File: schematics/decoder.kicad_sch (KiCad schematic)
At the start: 3 parts, among them U10 ATF22V10C-7, U11 74HC373, U9 ATF22V10C-7

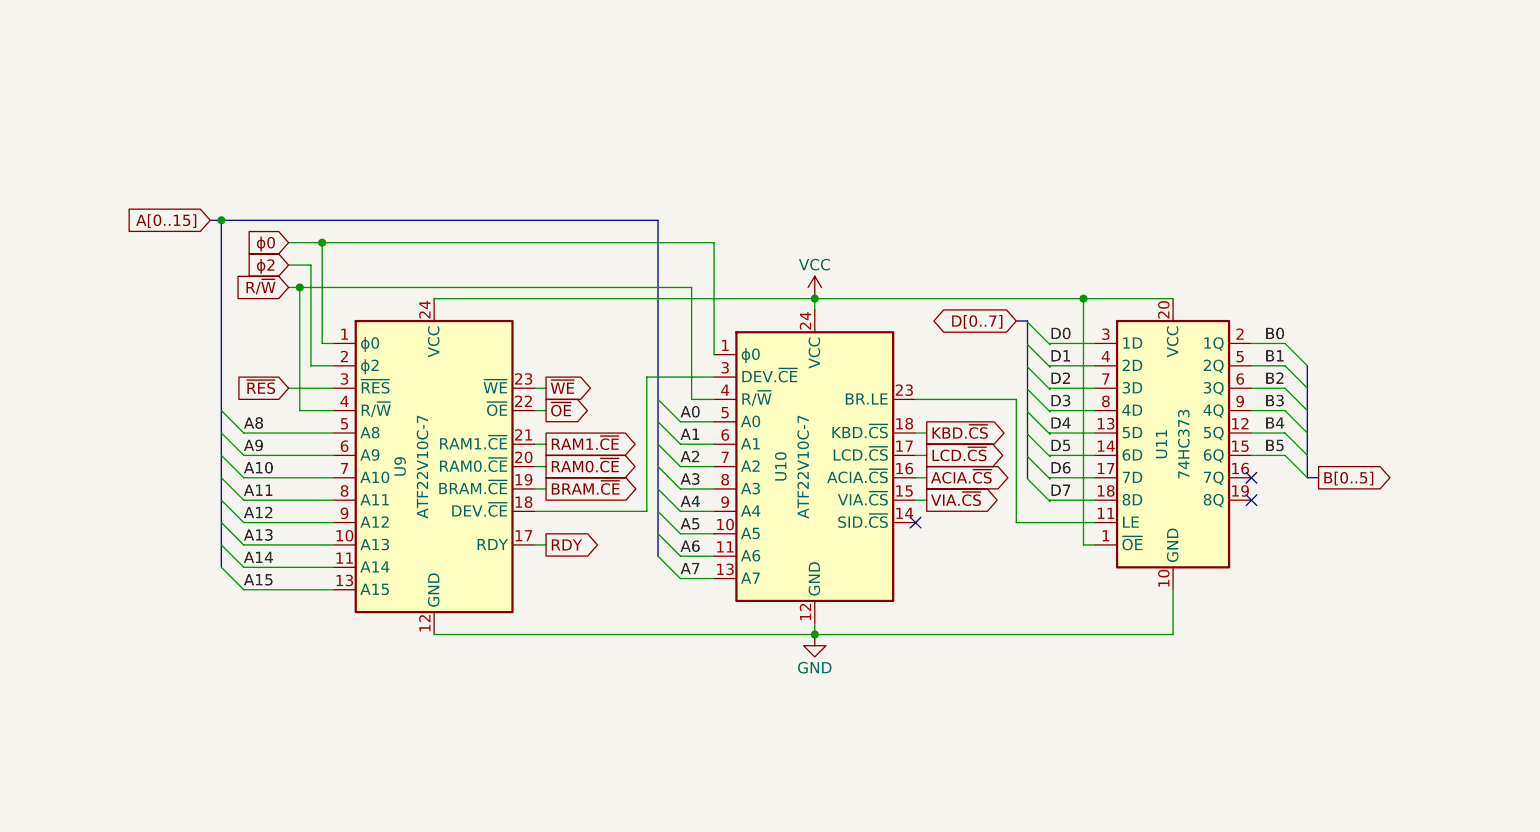
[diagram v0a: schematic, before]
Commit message: added back bus transceiver for devsel
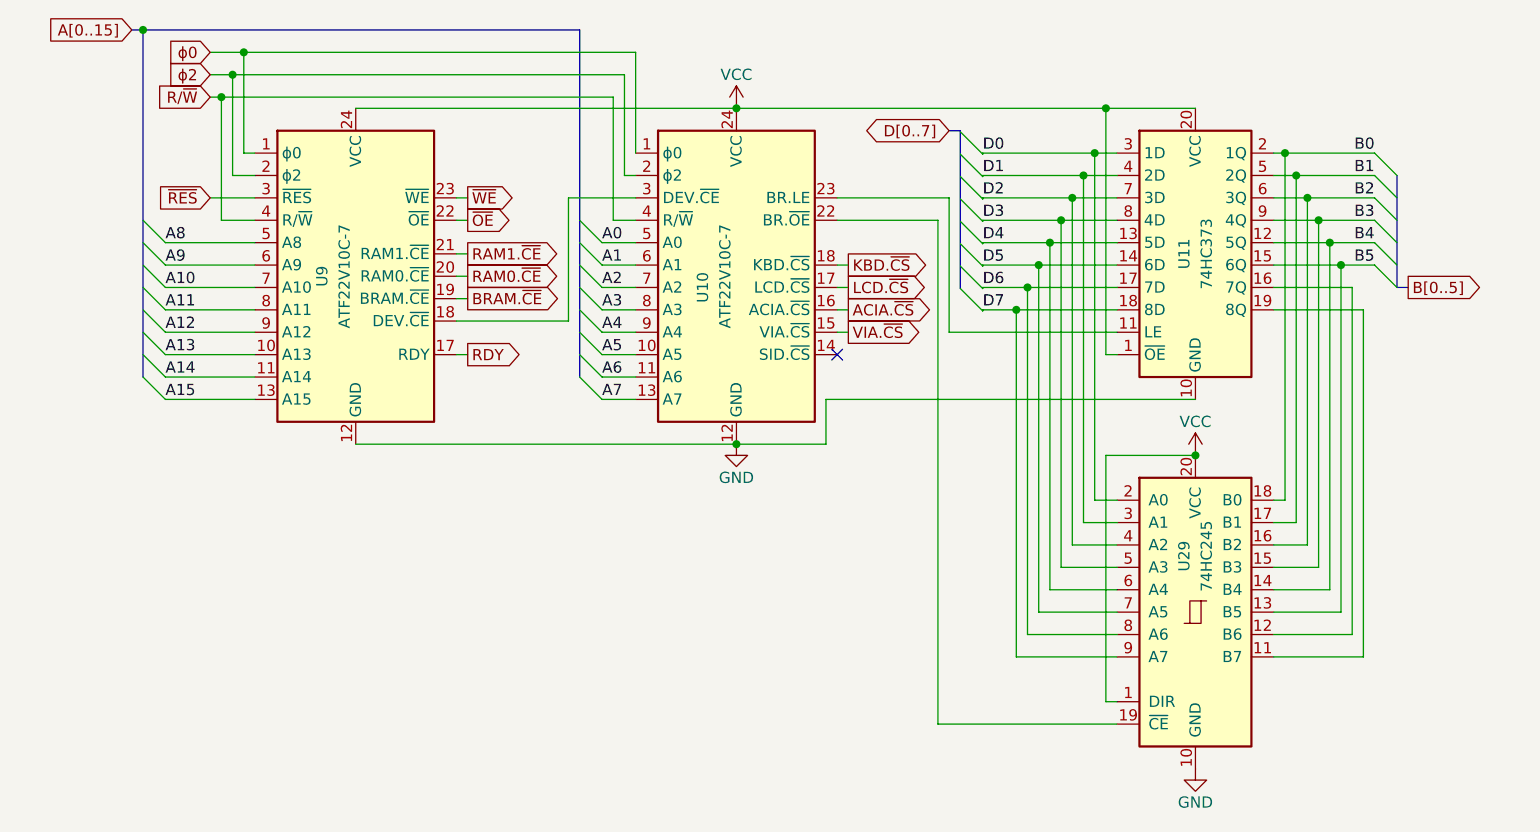
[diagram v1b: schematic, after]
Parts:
- added U29: 74HC245, symbol 74xx:74HC245
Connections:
- net B0: now also U29.18 (B0)
- net B1: now also U29.17 (B1)
- net B2: now also U29.16 (B2)
- net B3: now also U29.15 (B3)
- net B4: now also U29.14 (B4)
- net B5: now also U29.13 (B5)
- net D0: now also U29.2 (A0)
- net D1: now also U29.3 (A1)
- net D2: now also U29.4 (A2)
- net D3: now also U29.5 (A3)
- net D4: now also U29.6 (A4)
- net D5: now also U29.7 (A5)
- net D6: now also U29.8 (A6)
- net D7: now also U29.9 (A7)
- net GND: now also U29.10 (GND)
- net VCC: now also U29.1 (DIR), U29.20 (VCC)
- net ϕ2: now also U10.2 (ϕ2)
- net at U11.16 (7Q): now also U29.12 (B6)
- net at U11.19 (8Q): now also U29.11 (B7)
- net at U10.22 (BR.~{OE}): now also U29.19 (~{CE})
- no-connect marks 3 -> 1
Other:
- moved on the sheet: U11, U9

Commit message: fixing wiring
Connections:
- net BRAM.~{CE}: now also U9.16 (BRAM.~{CE}); no longer U9.19 (BRAM.~{CE})
- net GND: now also U29.1 (DIR)
- net RAM0.~{CE}: now also U9.17 (RAM0.~{CE}); no longer U9.20 (RAM0.~{CE})
- net RAM1.~{CE}: now also U9.18 (RAM1.~{CE}); no longer U9.21 (RAM1.~{CE})
- net RDY: now also U9.14 (RDY); no longer U9.17 (RDY)
- net VCC: no longer U29.1 (DIR)
- net ~{OE}: now also U9.19 (~{OE}); no longer U9.22 (~{OE})
- net ~{WE}: now also U9.20 (~{WE}); no longer U9.23 (~{WE})
- net at U11.11 (LE): now also U10.19 (BR.LE); no longer U10.23 (BR.LE)
- net at U10.20 (BR.~{OE}): now also U29.19 (~{CE})
- net at U10.22: no longer U29.19 (~{CE})
- net at U10.3 (DEV.~{CE}): now also U9.15 (DEV.~{CE}); no longer U9.18 (DEV.~{CE})
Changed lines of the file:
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@@
+	)
+	(junction
+		(at 186.69 143.51)
+		(diameter 0)
+		(color 0 0 0 0)
 	)
 	(junction
@@
 	(junction
 		(at 201.93 83.82)
-		(diameter 0)
-		(color 0 0 0 0)
-	)
-	(junction
-		(at 186.69 107.95)
 		(diameter 0)
 		(color 0 0 0 0)
@@
 	(wire
 		(pts
+			(xy 176.53 143.51) (xy 186.69 143.51)
+		)
+		(stroke
+			(width 0)
+			(type default)
+		)
+	)
+	(wire
+		(pts
 			(xy 162.56 76.2) (xy 173.99 76.2)
 		)
@@
 	(wire
 		(pts
-			(xy 176.53 107.95) (xy 186.69 107.95)
-		)
-		(stroke
-			(width 0)
-			(type default)
-		)
-	)
-	(wire
-		(pts
 			(xy 171.45 81.28) (xy 177.8 81.28)
 		)
@@
 	(wire
 		(pts
-			(xy 176.53 135.89) (xy 176.53 107.95)
-		)
-		(stroke
-			(width 0)
-			(type default)
-		)
-	)
-	(wire
-		(pts
 			(xy 177.8 130.81) (xy 166.37 130.81)
 		)
@@
 	(wire
 		(pts
-			(xy 158.75 78.74) (xy 146.05 78.74)
-		)
-		(stroke
-			(width 0)
-			(type default)
-		)
-	)
-	(wire
-		(pts
-			(xy 146.05 81.28) (xy 157.48 81.28)
+			(xy 158.75 82.55) (xy 146.05 82.55)
+		)
+		(stroke
+			(width 0)
+			(type default)
+		)
+	)
+	(wire
+		(pts
+			(xy 146.05 80.01) (xy 157.48 80.01)
 		)
 		(stroke
@@
 	(wire
 		(pts
-			(xy 157.48 81.28) (xy 157.48 138.43)
+			(xy 157.48 80.01) (xy 157.48 138.43)
 		)
 		(stroke
@@
 	(wire
 		(pts
-			(xy 158.75 93.98) (xy 158.75 78.74)
+			(xy 158.75 93.98) (xy 158.75 82.55)
 		)
 		(stroke
@@
 		)
 		(stroke
+			(width 0)
+			(type default)
+		)
+	)
+	(wire
+		(pts
+			(xy 176.53 135.89) (xy 176.53 143.51)
+		)
+		(stroke

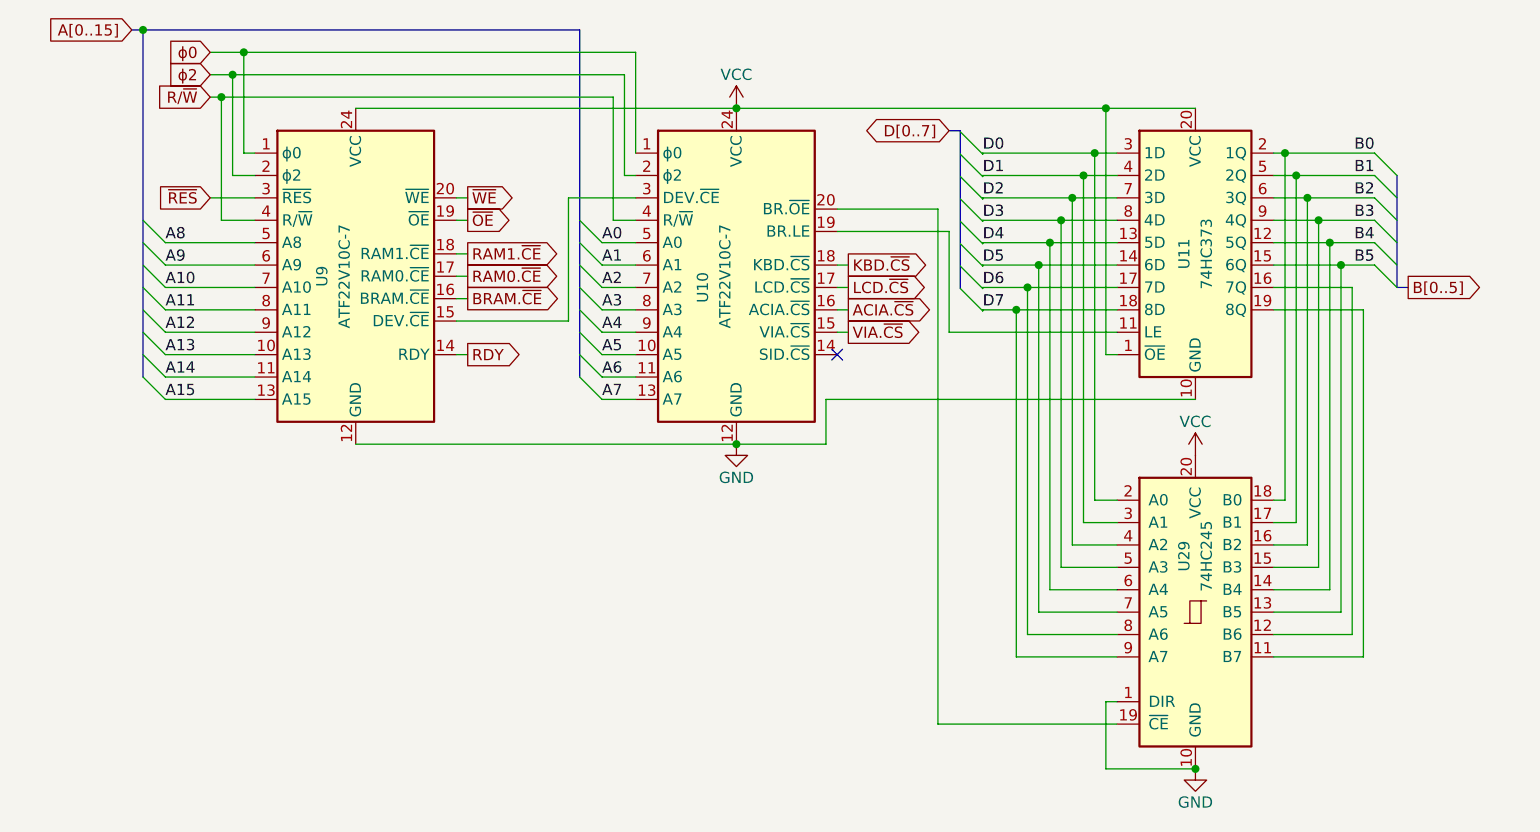
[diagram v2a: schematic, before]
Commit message: my keyboard needed a transceiver after all :(
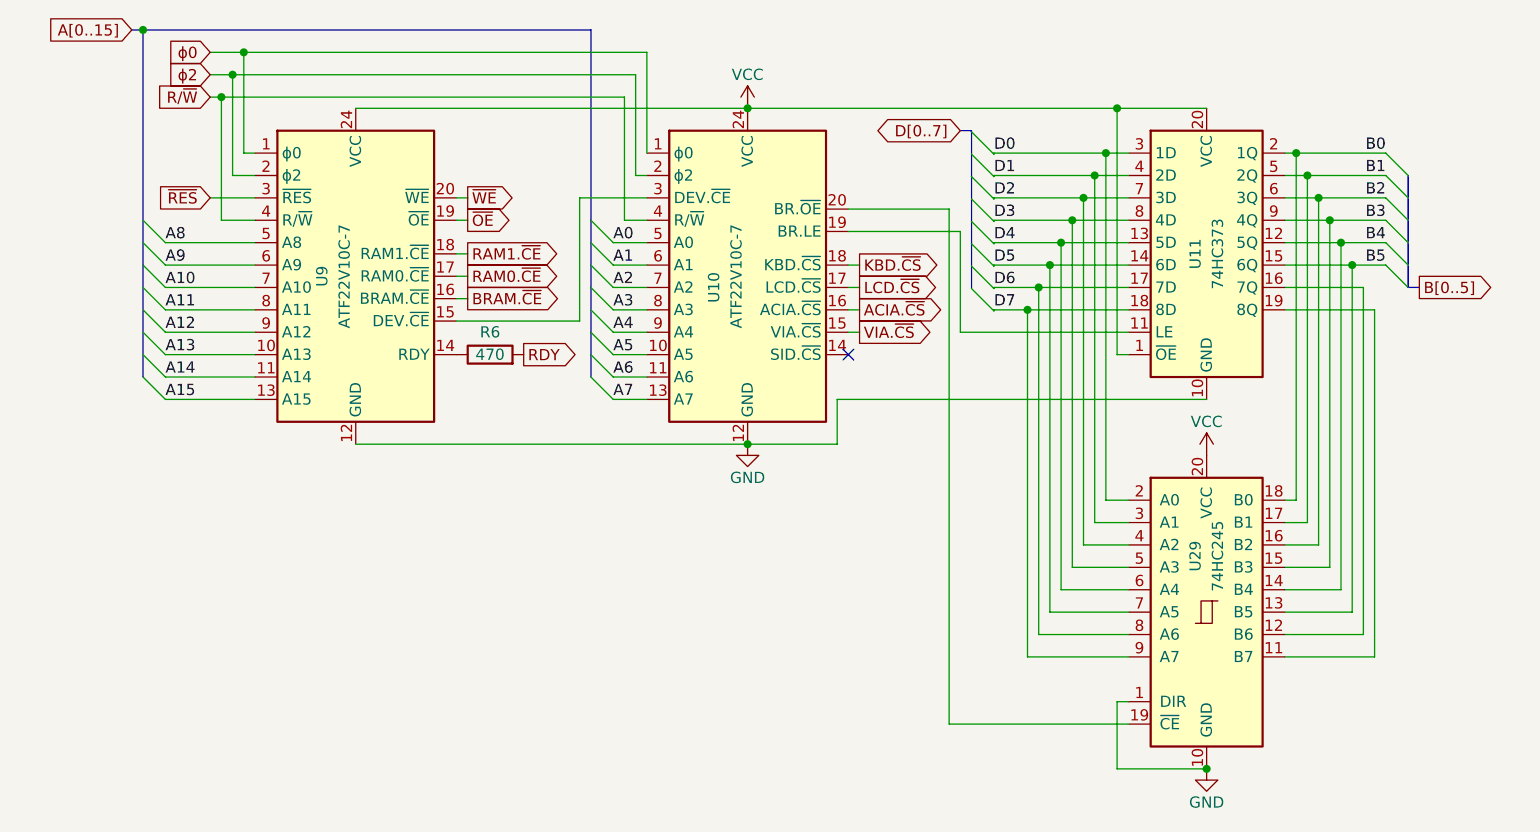
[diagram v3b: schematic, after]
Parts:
- added R6: 470, symbol Device:R
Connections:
- net RDY: now also R6.2; no longer U9.14 (RDY)
- new net: R6.1, U9.14 (RDY)
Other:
- moved on the sheet: U10, U11, U29

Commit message: clock improvements
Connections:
- net B1: now also U11.19 (2Q); no longer U11.5 (2Q)
- net B2: now also U11.5 (3Q); no longer U11.6 (3Q)
- net B3: now also U11.16 (4Q); no longer U11.9 (4Q)
- net B4: now also U11.6 (5Q); no longer U11.12 (5Q)
- net D1: now also U11.18 (2D); no longer U11.4 (2D)
- net D2: now also U11.4 (3D); no longer U11.7 (3D)
- net D3: now also U11.17 (4D); no longer U11.8 (4D)
- net D4: now also U11.7 (5D); no longer U11.13 (5D)
- net D6: now also U11.8 (7D); no longer U11.17 (7D)
- net D7: now also U11.13 (8D); no longer U11.18 (8D)
- net at U29.12 (B6): now also U11.9 (7Q); no longer U11.16 (7Q)
- net at U29.11 (B7): now also U11.12 (8Q); no longer U11.19 (8Q)
- net ϕ0 renamed ϕ0.1
- net ϕ2 renamed ϕ2.1
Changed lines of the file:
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@@
 		)
 	)
-	(global_label "ϕ2"
+	(global_label "ϕ2.1"
 		(shape input)
 		(at 74.93 64.77 180)
@@
 		)
 		(property "Intersheetrefs" "${INTERSHEET_REFS}"
-			(at 69.4048 64.77 0)
+			(at 67.5905 64.77 0)
 			(hide yes)
 			(show_name no)
@@
 		)
 	)
-	(global_label "ϕ0"
+	(global_label "ϕ0.1"
 		(shape input)
 		(at 74.93 62.23 180)
@@
 		)
 		(property "Intersheetrefs" "${INTERSHEET_REFS}"
-			(at 69.4048 62.23 0)
+			(at 67.5905 62.23 0)
 			(hide yes)
 			(show_name no)

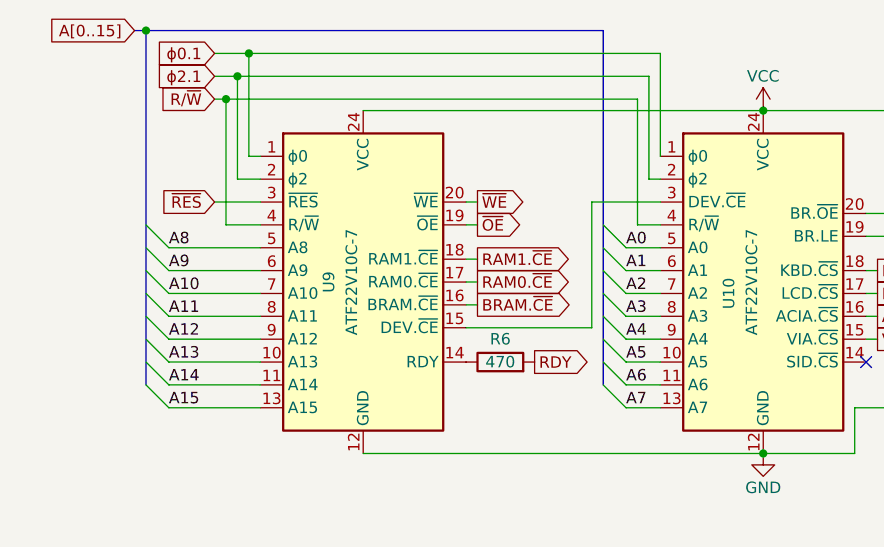
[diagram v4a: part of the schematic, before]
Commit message: ditched phi0, dropped to 6MHz
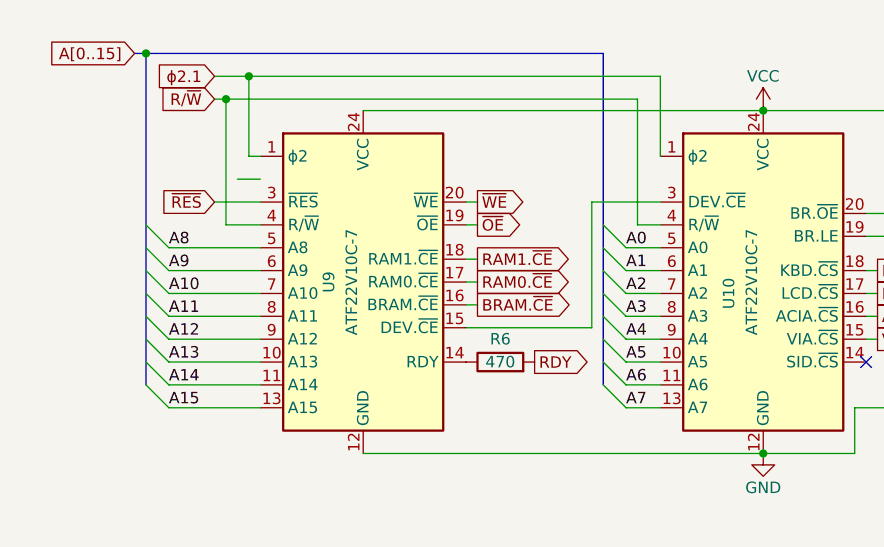
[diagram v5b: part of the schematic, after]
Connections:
- net ϕ0.1 is gone; now on net ϕ2.1: U10.1 (ϕ2), U9.1 (ϕ2)
- net ϕ2.1: no longer U10.2 (ϕ2), U9.2 (ϕ2)
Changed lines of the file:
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@@
 	)
 	(junction
-		(at 78.74 62.23)
+		(at 78.74 64.77)
 		(diameter 0)
 		(color 0 0 0 0)
@@
 	)
 	(junction
-		(at 77.47 64.77)
-		(diameter 0)
-		(color 0 0 0 0)
-	)
-	(junction
 		(at 171.45 83.82)
 		(diameter 0)
@@
 	)
 	(junction
-		(at 67.31 59.69)
+		(at 67.31 62.23)
 		(diameter 0)
 		(color 0 0 0 0)
@@
 	(wire
 		(pts
-			(xy 124.46 62.23) (xy 124.46 73.66)
+			(xy 124.46 64.77) (xy 124.46 73.66)
 		)
 		(stroke
@@
 	(wire
 		(pts
-			(xy 74.93 64.77) (xy 77.47 64.77)
-		)
-		(stroke
-			(width 0)
-			(type default)
-		)
-	)
-	(wire
-		(pts
 			(xy 170.18 86.36) (xy 179.07 86.36)
 		)
@@
 	(wire
 		(pts
-			(xy 77.47 64.77) (xy 77.47 76.2)
-		)
-		(stroke
-			(width 0)
-			(type default)
-		)
-	)
-	(wire
-		(pts
 			(xy 175.26 76.2) (xy 175.26 115.57)
 		)
@@
 	(bus
 		(pts
-			(xy 67.31 59.69) (xy 118.11 59.69)
+			(xy 67.31 62.23) (xy 118.11 62.23)
 		)
 		(stroke
@@
 	(bus
 		(pts
-			(xy 67.31 59.69) (xy 67.31 99.06)
+			(xy 67.31 62.23) (xy 67.31 99.06)
 		)
 		(stroke
@@
 	(wire
 		(pts
-			(xy 78.74 62.23) (xy 78.74 73.66)
+			(xy 78.74 64.77) (xy 78.74 73.66)
 		)
 		(stroke
@@
 	(wire
 		(pts
-			(xy 78.74 62.23) (xy 124.46 62.23)
+			(xy 78.74 64.77) (xy 124.46 64.77)
 		)
 		(stroke
@@
 	(wire
 		(pts
-			(xy 123.19 76.2) (xy 123.19 64.77)
-		)
-		(stroke
-			(width 0)
-			(type default)
-		)
-	)
-	(wire
-		(pts
 			(xy 201.93 81.28) (xy 208.28 81.28)
 		)
@@
 	(wire
 		(pts
-			(xy 74.93 62.23) (xy 78.74 62.23)
+			(xy 74.93 64.77) (xy 78.74 64.77)
 		)
 		(stroke
@@
 	(wire
 		(pts
-			(xy 123.19 76.2) (xy 124.46 76.2)
-		)
-		(stroke
-			(width 0)
-			(type default)
-		)
-	)
-	(wire
-		(pts
-			(xy 123.19 64.77) (xy 77.47 64.77)
-		)
-		(stroke
-			(width 0)
-			(type default)
-		)
-	)
-	(wire
-		(pts
 			(xy 196.85 120.65) (xy 201.93 120.65)
 		)
@@
 	(bus
 		(pts
-			(xy 118.11 59.69) (xy 118.11 99.06)
+			(xy 118.11 62.23) (xy 118.11 99.06)
 		)
 		(stroke
@@
 	(bus
 		(pts
-			(xy 67.31 59.69) (xy 66.04 59.69)
+			(xy 67.31 62.23) (xy 66.04 62.23)
 		)
 		(stroke
@@
 	(global_label "A[0..15]"
 		(shape input)
-		(at 66.04 59.69 180)
+		(at 66.04 62.23 180)
 		(fields_autoplaced yes)
 		(effects
@@
 		)
 		(property "Intersheetrefs" "${INTERSHEET_REFS}"
-			(at 55.4347 59.69 0)
+			(at 55.4347 62.23 0)
 			(hide yes)
 			(show_name no)
@@
 		)
 	)
-	(global_label "ϕ2.1"
-		(shape input)
-		(at 74.93 64.77 180)
-		(fields_autoplaced yes)
-		(effects
-			(font
-				(size 1.27 1.27)
-			)
-			(justify right)
-		)
-		(property "Intersheetrefs" "${INTERSHEET_REFS}"
-			(at 67.5905 64.77 0)
-			(hide yes)
-			(show_name no)
-			(do_not_autoplace no)
-			(effects
-				(font
-					(size 1.27 1.27)
-				)
-				(justify right)
-			)
-		)
-	)
 	(global_label "~{WE}"
 		(shape output)
@@
 		)
 	)
-	(global_label "ϕ0.1"
+	(global_label "ϕ2.1"
 		(shape input)
-		(at 74.93 62.23 180)
+		(at 74.93 64.77 180)
 		(fields_autoplaced yes)
 		(effects
@@
 		)
 		(property "Intersheetrefs" "${INTERSHEET_REFS}"
-			(at 67.5905 62.23 0)
+			(at 67.5905 64.77 0)
 			(hide yes)
 			(show_name no)
